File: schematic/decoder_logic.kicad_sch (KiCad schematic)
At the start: 2 parts, among them U5 74LS138, U6 74LS138

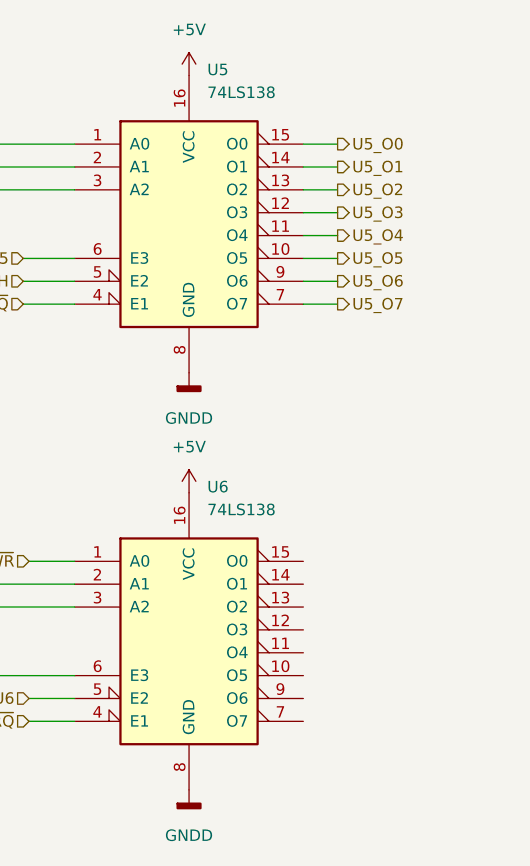
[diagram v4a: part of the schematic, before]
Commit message: added u6 decoder lines, renamed a few lines to make sense to there destination.
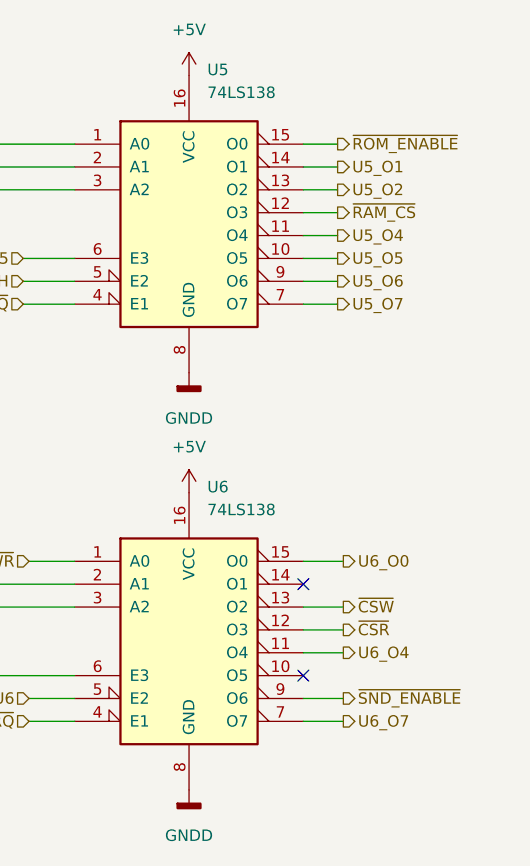
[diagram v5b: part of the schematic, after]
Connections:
- net U6_O4: now reaches U6.11 (O4)
- net ~{CSR}: now reaches U6.12 (O3)
- net ~{CSW}: now reaches U6.13 (O2)
- net U6_O0: now reaches U6.15 (O0)
- net U6_O7: now reaches U6.7 (O7)
- net ~{SND_ENABLE}: now reaches U6.9 (O6)
- net U5_O0 renamed ~{ROM_ENABLE}
- net U5_O3 renamed ~{RAM_CS}
- no-connect marks 0 -> 2
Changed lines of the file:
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@@
 (kicad_sch (version 20211123) (generator eeschema)
   (paper "A4")
+  (no_connect (at 144.78 136.525))
+  (no_connect (at 144.78 126.365))
   (bus_entry (at 99.695 139.065) (size 2.54 -2.54)
     (stroke (width 0) (type default) (color 0 0 0 0))
@@
     (stroke (width 0) (type default) (color 0 0 0 0))
   )
+  (wire (pts (xy 144.78 131.445) (xy 149.225 131.445))
+    (stroke (width 0) (type default) (color 0 0 0 0))
+  )
   (wire (pts (xy 144.78 80.01) (xy 148.59 80.01))
     (stroke (width 0) (type default) (color 0 0 0 0))
   )
+  (wire (pts (xy 144.78 123.825) (xy 149.225 123.825))
+    (stroke (width 0) (type default) (color 0 0 0 0))
+  )
   (bus (pts (xy 99.695 131.445) (xy 99.695 139.065))
     (stroke (width 0) (type default) (color 0 0 0 0))
@@
     (stroke (width 0) (type default) (color 0 0 0 0))
   )
+  (wire (pts (xy 144.78 128.905) (xy 149.225 128.905))
+    (stroke (width 0) (type default) (color 0 0 0 0))
+  )
   (wire (pts (xy 102.235 82.55) (xy 119.38 82.55))
     (stroke (width 0) (type default) (color 0 0 0 0))
@@
     (stroke (width 0) (type default) (color 0 0 0 0))
   )
+  (wire (pts (xy 144.78 141.605) (xy 149.225 141.605))
+    (stroke (width 0) (type default) (color 0 0 0 0))
+  )
   (wire (pts (xy 102.235 126.365) (xy 119.38 126.365))
     (stroke (width 0) (type default) (color 0 0 0 0))
@@
     (stroke (width 0) (type default) (color 0 0 0 0))
   )
+  (wire (pts (xy 144.78 139.065) (xy 149.225 139.065))
+    (stroke (width 0) (type default) (color 0 0 0 0))
+  )
   (wire (pts (xy 144.78 85.09) (xy 148.59 85.09))
     (stroke (width 0) (type default) (color 0 0 0 0))
@@
     (stroke (width 0) (type default) (color 0 0 0 0))
   )
+  (wire (pts (xy 144.78 133.985) (xy 149.225 133.985))
+    (stroke (width 0) (type default) (color 0 0 0 0))
+  )
   (wire (pts (xy 114.3 141.605) (xy 119.38 141.605))
     (stroke (width 0) (type default) (color 0 0 0 0))
@@
     (effects (font (size 1.27 1.27)) (justify left))
   )
+  (hierarchical_label "U6_O7" (shape output) (at 149.225 141.605 0)
+    (effects (font (size 1.27 1.27)) (justify left))
+  )
   (hierarchical_label "E3_U5" (shape input) (at 113.665 90.17 180)
     (effects (font (size 1.27 1.27)) (justify right))
@@
     (effects (font (size 1.27 1.27)) (justify right))
   )
-  (hierarchical_label "U5_O3" (shape output) (at 148.59 85.09 0)
+  (hierarchical_label "~{RAM_CS}" (shape output) (at 148.59 85.09 0)
     (effects (font (size 1.27 1.27)) (justify left))
   )
@@
     (effects (font (size 1.27 1.27)) (justify right))
   )
+  (hierarchical_label "U6_O4" (shape output) (at 149.225 133.985 0)
+    (effects (font (size 1.27 1.27)) (justify left))
+  )
   (hierarchical_label "U5_O4" (shape output) (at 148.59 87.63 0)
     (effects (font (size 1.27 1.27)) (justify left))
@@
     (effects (font (size 1.27 1.27)) (justify left))
   )
+  (hierarchical_label "~{SND_ENABLE}" (shape output) (at 149.225 139.065 0)
+    (effects (font (size 1.27 1.27)) (justify left))
+  )
+  (hierarchical_label "U6_O0" (shape output) (at 149.225 123.825 0)
+    (effects (font (size 1.27 1.27)) (justify left))
+  )
+  (hierarchical_label "~{CSW}" (shape output) (at 149.225 128.905 0)
+    (effects (font (size 1.27 1.27)) (justify left))
+  )
   (hierarchical_label "A[0..15]" (shape input) (at 84.455 77.47 180)
     (effects (font (size 1.27 1.27)) (justify right))
@@
     (effects (font (size 1.27 1.27)) (justify right))
   )
-  (hierarchical_label "U5_O0" (shape output) (at 148.59 77.47 0)
-    (effects (font (size 1.27 1.27)) (justify left))
-  )
+  (hierarchical_label "~{ROM_ENABLE}" (shape output) (at 148.59 77.47 0)
+    (effects (font (size 1.27 1.27)) (justify left))
+  )
+  (hierarchical_label "~{CSR}" (shape output) (at 149.225 131.445 0)
+    (effects (font (size 1.27 1.27)) (justify left))
+  )

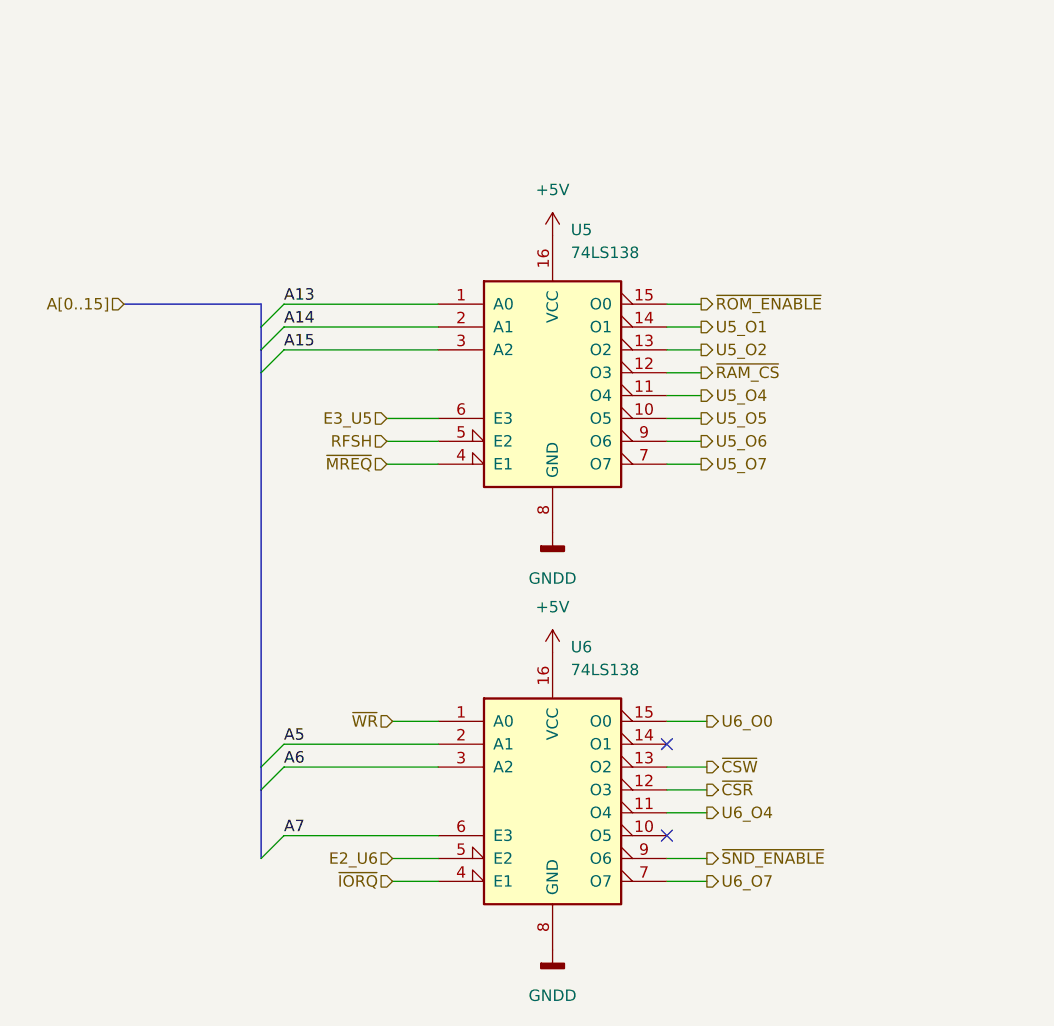
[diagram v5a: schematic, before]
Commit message: altered and did some cleanup of the way the wires were run. Finished expansion port routes to rf modulator. Added ext_psu for future external power supply design (will be an off the shelf psu block).
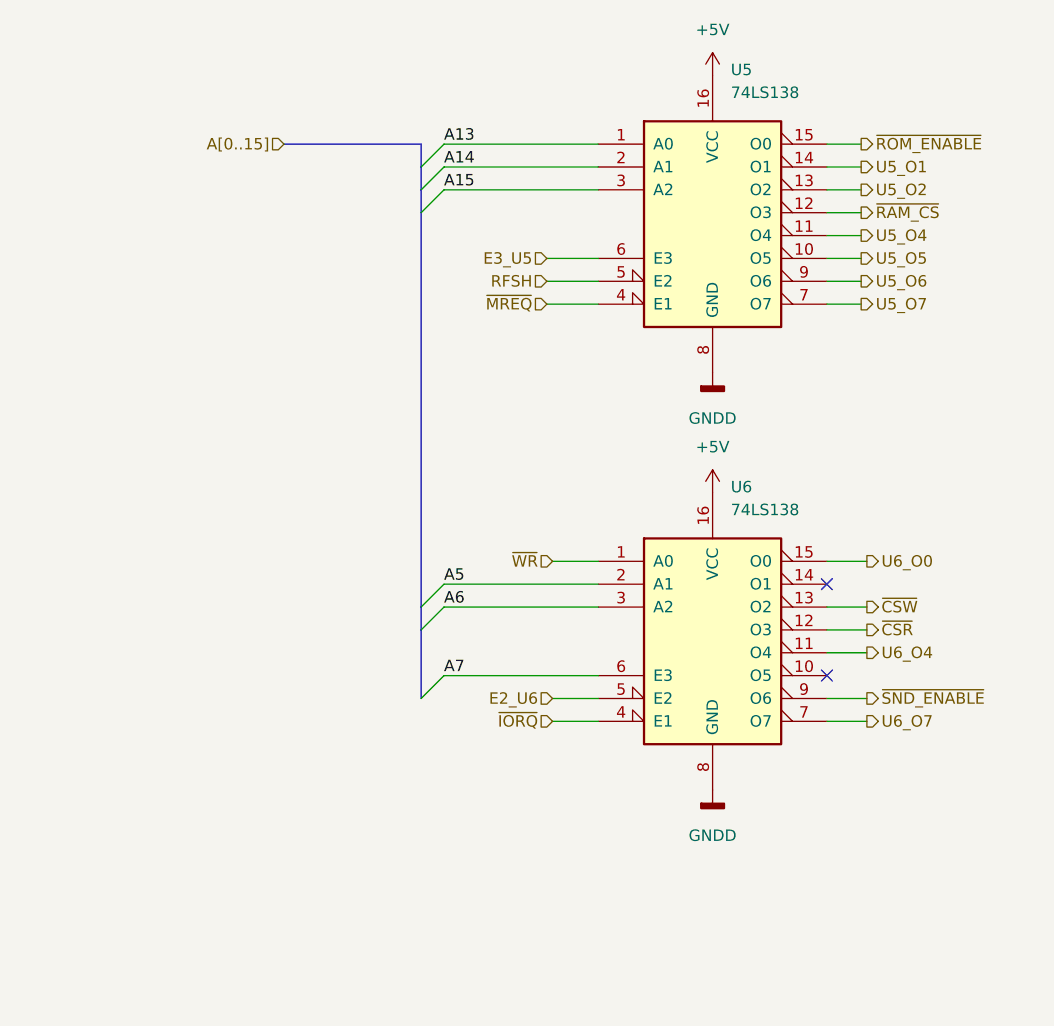
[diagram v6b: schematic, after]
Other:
- moved on the sheet: U5, U6

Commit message: all lines renamed, based most of the names from the coleco adam schematic. CS cart lines are my own, and the rest are from the wiki schematic for the controller... those will need to be checked.
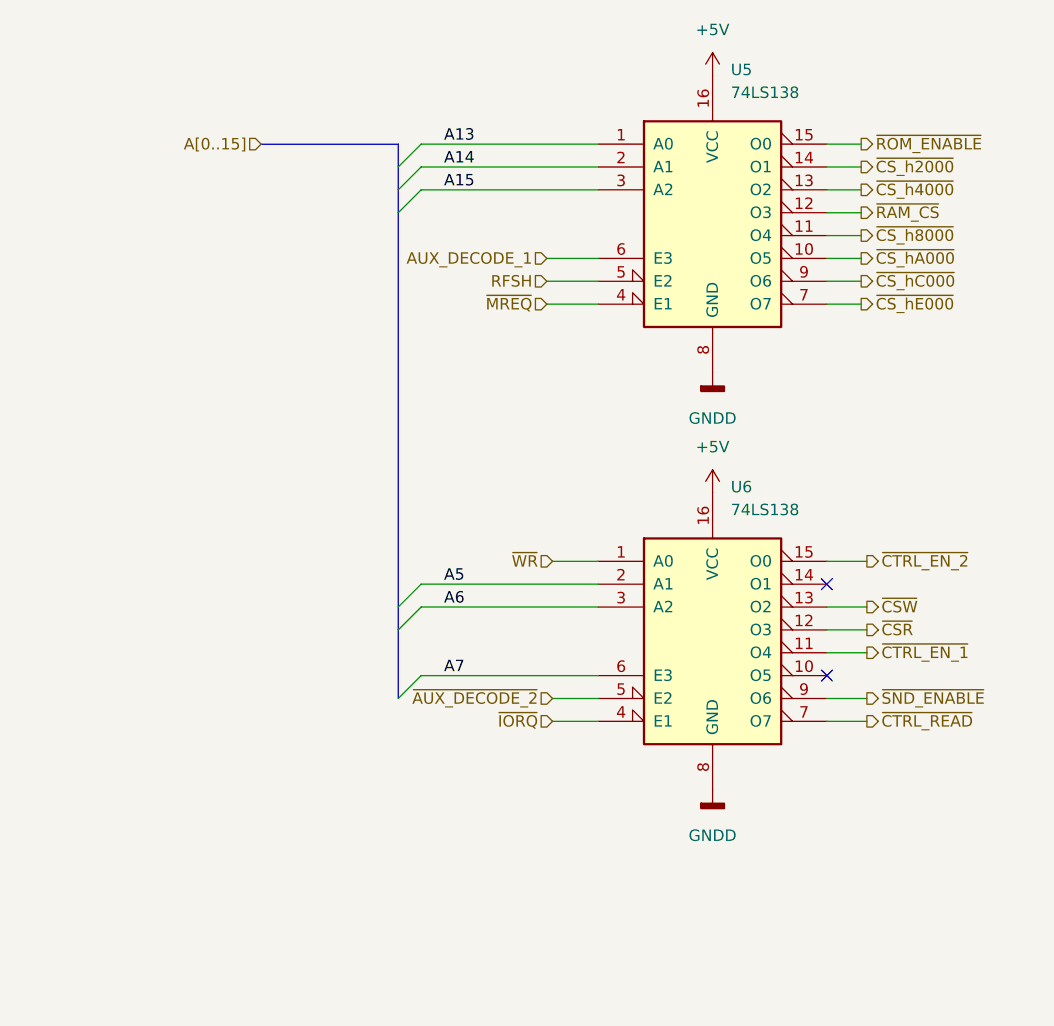
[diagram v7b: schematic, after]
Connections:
- net E2_U6 renamed ~{AUX_DECODE_2}
- net E3_U5 renamed AUX_DECODE_1
- net U5_O1 renamed ~{CS_h2000}
- net U5_O2 renamed ~{CS_h4000}
- net U5_O4 renamed ~{CS_h8000}
- net U5_O5 renamed ~{CS_hA000}
- net U5_O6 renamed ~{CS_hC000}
- net U5_O7 renamed ~{CS_hE000}
- net U6_O0 renamed ~{CTRL_EN_2}
- net U6_O4 renamed ~{CTRL_EN_1}
- net U6_O7 renamed ~{CTRL_READ}
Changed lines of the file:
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@@
   (no_connect (at 162.56 118.745))
   (no_connect (at 162.56 108.585))
-  (bus_entry (at 117.475 121.285) (size 2.54 -2.54)
+  (bus_entry (at 114.935 121.285) (size 2.54 -2.54)
     (stroke (width 0) (type default) (color 0 0 0 0))
   )
-  (bus_entry (at 117.475 64.77) (size 2.54 -2.54)
+  (bus_entry (at 114.935 64.77) (size 2.54 -2.54)
     (stroke (width 0) (type default) (color 0 0 0 0))
   )
-  (bus_entry (at 117.475 111.125) (size 2.54 -2.54)
+  (bus_entry (at 114.935 111.125) (size 2.54 -2.54)
     (stroke (width 0) (type default) (color 0 0 0 0))
   )
-  (bus_entry (at 117.475 62.23) (size 2.54 -2.54)
+  (bus_entry (at 114.935 62.23) (size 2.54 -2.54)
     (stroke (width 0) (type default) (color 0 0 0 0))
   )
-  (bus_entry (at 117.475 67.31) (size 2.54 -2.54)
+  (bus_entry (at 114.935 67.31) (size 2.54 -2.54)
     (stroke (width 0) (type default) (color 0 0 0 0))
   )
-  (bus_entry (at 117.475 113.665) (size 2.54 -2.54)
+  (bus_entry (at 114.935 113.665) (size 2.54 -2.54)
     (stroke (width 0) (type default) (color 0 0 0 0))
   )
-  (bus (pts (xy 117.475 59.69) (xy 102.235 59.69))
+  (bus (pts (xy 114.935 59.69) (xy 99.695 59.69))
     (stroke (width 0) (type default) (color 0 0 0 0))
   )
-  (bus (pts (xy 117.475 67.31) (xy 117.475 111.125))
+  (bus (pts (xy 114.935 67.31) (xy 114.935 111.125))
     (stroke (width 0) (type default) (color 0 0 0 0))
   )
@@
     (stroke (width 0) (type default) (color 0 0 0 0))
   )
-  (bus (pts (xy 117.475 67.31) (xy 117.475 64.77))
+  (bus (pts (xy 114.935 67.31) (xy 114.935 64.77))
     (stroke (width 0) (type default) (color 0 0 0 0))
   )
-  (wire (pts (xy 120.015 62.23) (xy 137.16 62.23))
+  (wire (pts (xy 117.475 62.23) (xy 137.16 62.23))
     (stroke (width 0) (type default) (color 0 0 0 0))
   )
-  (wire (pts (xy 120.015 59.69) (xy 137.16 59.69))
+  (wire (pts (xy 117.475 59.69) (xy 137.16 59.69))
     (stroke (width 0) (type default) (color 0 0 0 0))
   )
-  (bus (pts (xy 117.475 62.23) (xy 117.475 59.69))
+  (bus (pts (xy 114.935 62.23) (xy 114.935 59.69))
     (stroke (width 0) (type default) (color 0 0 0 0))
   )
@@
     (stroke (width 0) (type default) (color 0 0 0 0))
   )
-  (bus (pts (xy 117.475 113.665) (xy 117.475 121.285))
+  (bus (pts (xy 114.935 113.665) (xy 114.935 121.285))
     (stroke (width 0) (type default) (color 0 0 0 0))
   )
@@
     (stroke (width 0) (type default) (color 0 0 0 0))
   )
-  (wire (pts (xy 120.015 64.77) (xy 137.16 64.77))
+  (wire (pts (xy 117.475 64.77) (xy 137.16 64.77))
     (stroke (width 0) (type default) (color 0 0 0 0))
   )
@@
     (stroke (width 0) (type default) (color 0 0 0 0))
   )
-  (bus (pts (xy 117.475 111.125) (xy 117.475 113.665))
+  (bus (pts (xy 114.935 111.125) (xy 114.935 113.665))
     (stroke (width 0) (type default) (color 0 0 0 0))
   )
@@
     (stroke (width 0) (type default) (color 0 0 0 0))
   )
-  (wire (pts (xy 120.015 108.585) (xy 137.16 108.585))
+  (wire (pts (xy 117.475 108.585) (xy 137.16 108.585))
     (stroke (width 0) (type default) (color 0 0 0 0))
   )
@@
     (stroke (width 0) (type default) (color 0 0 0 0))
   )
-  (wire (pts (xy 120.015 118.745) (xy 137.16 118.745))
+  (wire (pts (xy 117.475 118.745) (xy 137.16 118.745))
     (stroke (width 0) (type default) (color 0 0 0 0))
   )
@@
     (stroke (width 0) (type default) (color 0 0 0 0))
   )
-  (bus (pts (xy 117.475 64.77) (xy 117.475 62.23))
+  (bus (pts (xy 114.935 64.77) (xy 114.935 62.23))
     (stroke (width 0) (type default) (color 0 0 0 0))
   )
@@
     (stroke (width 0) (type default) (color 0 0 0 0))
   )
-  (wire (pts (xy 120.015 111.125) (xy 137.16 111.125))
+  (wire (pts (xy 117.475 111.125) (xy 137.16 111.125))
     (stroke (width 0) (type default) (color 0 0 0 0))
   )
@@
     (effects (font (size 1.27 1.27)) (justify left bottom))
   )
-  (hierarchical_label "U5_O6" (shape output) (at 166.37 74.93 0)
+  (hierarchical_label "~{CS_hC000}" (shape output) (at 166.37 74.93 0)
     (effects (font (size 1.27 1.27)) (justify left))
   )
-  (hierarchical_label "U6_O7" (shape output) (at 167.005 123.825 0)
+  (hierarchical_label "~{CTRL_READ}" (shape output) (at 167.005 123.825 0)
     (effects (font (size 1.27 1.27)) (justify left))
   )
-  (hierarchical_label "E3_U5" (shape input) (at 131.445 72.39 180)
+  (hierarchical_label "AUX_DECODE_1" (shape input) (at 131.445 72.39 180)
     (effects (font (size 1.27 1.27)) (justify right))
   )
@@
     (effects (font (size 1.27 1.27)) (justify right))
   )
-  (hierarchical_label "U5_O7" (shape output) (at 166.37 77.47 0)
+  (hierarchical_label "~{CS_hE000}" (shape output) (at 166.37 77.47 0)
     (effects (font (size 1.27 1.27)) (justify left))
   )
-  (hierarchical_label "U5_O2" (shape output) (at 166.37 64.77 0)
+  (hierarchical_label "~{CS_h4000}" (shape output) (at 166.37 64.77 0)
     (effects (font (size 1.27 1.27)) (justify left))
   )
@@
     (effects (font (size 1.27 1.27)) (justify left))
   )
-  (hierarchical_label "E2_U6" (shape input) (at 132.08 121.285 180)
+  (hierarchical_label "~{AUX_DECODE_2}" (shape input) (at 132.08 121.285 180)
     (effects (font (size 1.27 1.27)) (justify right))
   )
@@
     (effects (font (size 1.27 1.27)) (justify right))
   )
-  (hierarchical_label "U6_O4" (shape output) (at 167.005 116.205 0)
+  (hierarchical_label "~{CTRL_EN_1}" (shape output) (at 167.005 116.205 0)
     (effects (font (size 1.27 1.27)) (justify left))
   )
-  (hierarchical_label "U5_O4" (shape output) (at 166.37 69.85 0)
+  (hierarchical_label "~{CS_h8000}" (shape output) (at 166.37 69.85 0)
     (effects (font (size 1.27 1.27)) (justify left))
   )
-  (hierarchical_label "U5_O5" (shape output) (at 166.37 72.39 0)
+  (hierarchical_label "~{CS_hA000}" (shape output) (at 166.37 72.39 0)
     (effects (font (size 1.27 1.27)) (justify left))
   )
-  (hierarchical_label "U5_O1" (shape output) (at 166.37 62.23 0)
+  (hierarchical_label "~{CS_h2000}" (shape output) (at 166.37 62.23 0)
     (effects (font (size 1.27 1.27)) (justify left))
   )
@@
     (effects (font (size 1.27 1.27)) (justify left))
   )
-  (hierarchical_label "U6_O0" (shape output) (at 167.005 106.045 0)
+  (hierarchical_label "~{CTRL_EN_2}" (shape output) (at 167.005 106.045 0)
     (effects (font (size 1.27 1.27)) (justify left))
   )
@@
     (effects (font (size 1.27 1.27)) (justify left))
   )
-  (hierarchical_label "A[0..15]" (shape input) (at 102.235 59.69 180)
+  (hierarchical_label "A[0..15]" (shape input) (at 99.695 59.69 180)
     (effects (font (size 1.27 1.27)) (justify right))
   )

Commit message: adjusted size of the sheets. added pcb version to the rev field. F.0... the 0 is for future fixes on my end. RF PCB is E.0.
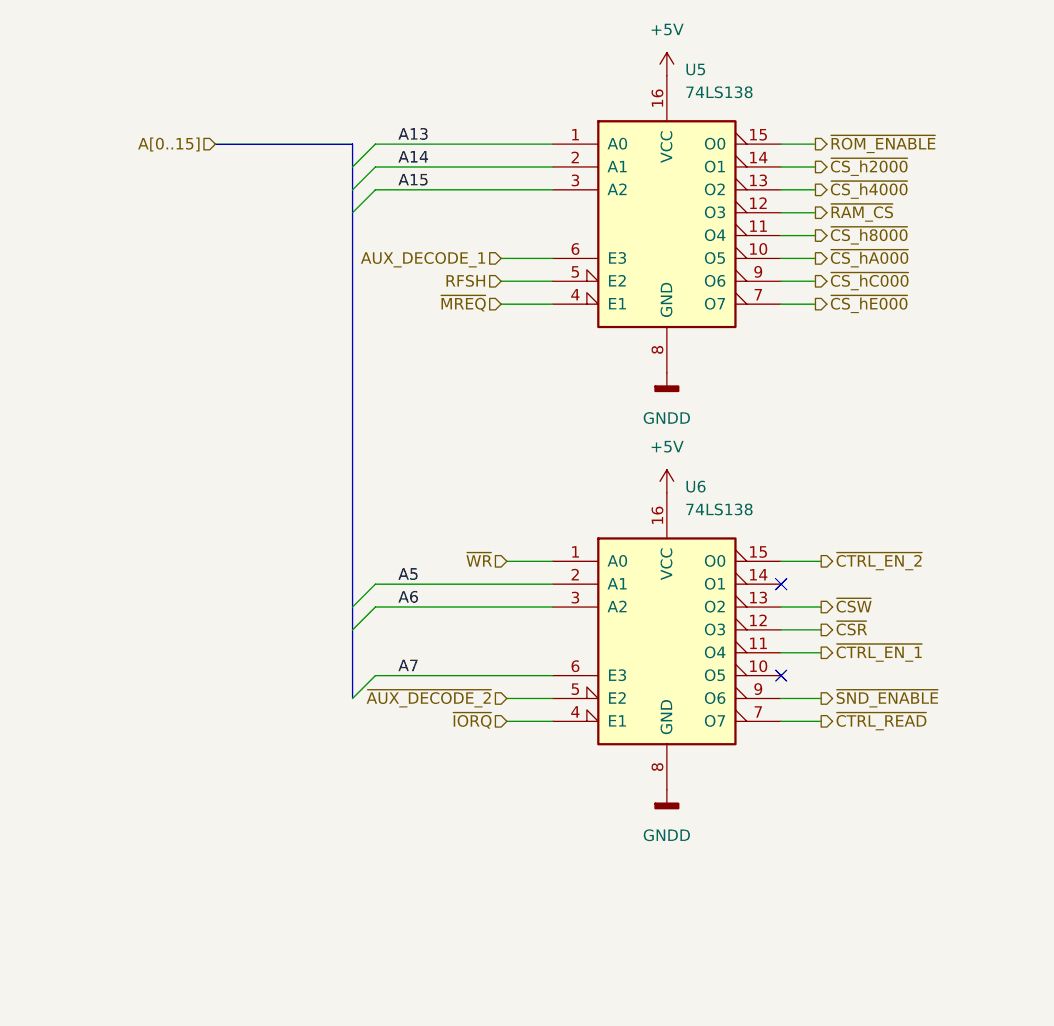
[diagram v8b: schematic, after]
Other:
- title: (none) -> Colecovision Schematic
- moved on the sheet: U5, U6
